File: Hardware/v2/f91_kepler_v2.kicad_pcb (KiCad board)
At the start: 2 copper layers, 25 x 27 mm, 89 parts, among them J1 LS013B7DH03 FPC, Q1 FS8205A, SW1 BTN1/BSL, SW2 BTN2, SW3 BTN3, U1 CC2652R7RGZ, U2 BQ51050B, U3 DW01A, U4 XC6206P302MR, U5 LIS2DW12, U6 DRV2605L, U7 ST25DV04K, Y1 48MHz FA-128, Y2 32.768kHz FC-135

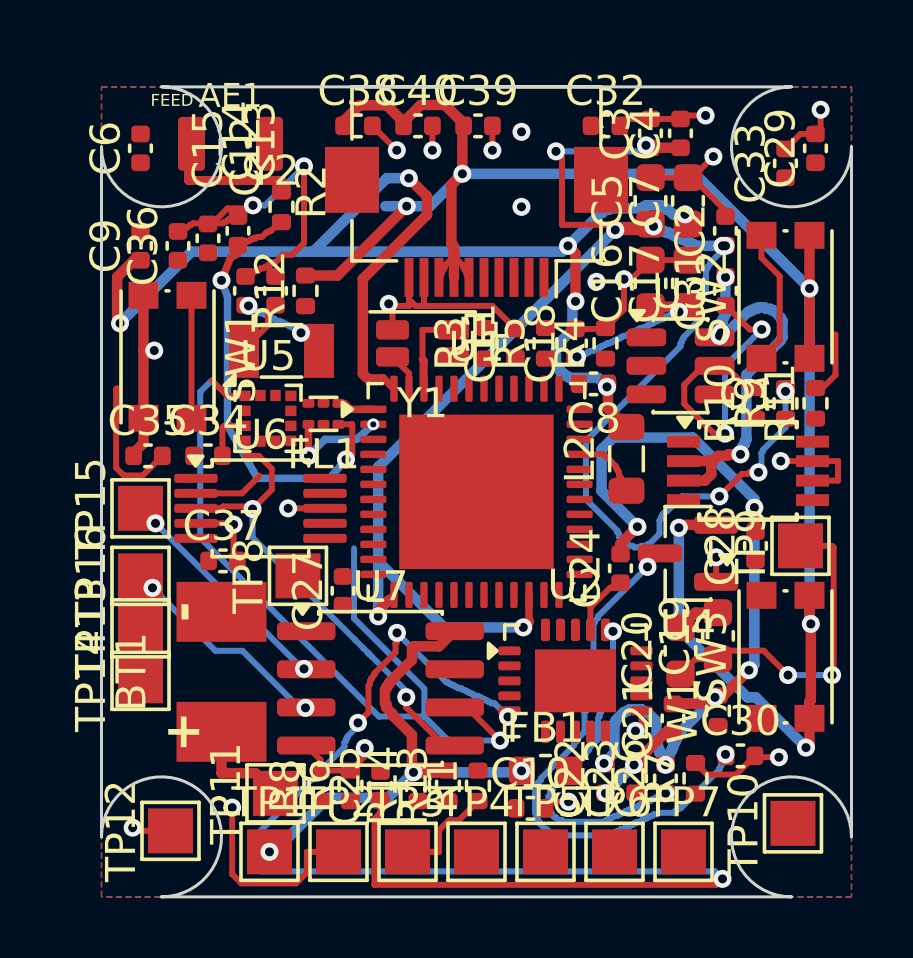
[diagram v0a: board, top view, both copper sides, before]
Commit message: feat(hw/v2): pin remap + placement surgery, routing at 54% remaining ratsnest
- re-pin (CC2652 IOC mux): LCD MOSI/SCLK/CS/DISP/EXTCOMIN -> DIO_27-30/26
  (top edge, face J1), BTN_1 -> DIO_0, BTN_3 -> DIO_20, UART_RX/TX ->
  DIO_9/10, ACC_INT2 -> DIO_11; schematic + board + kepler_config.h
  (KEPLER_BOARD_V2 block) + PINMAP.md all in sync, ERC 0
- surgery: U2 +0.7 (U1-U2 channel 0.35 -> 1.05mm), FB1/C22/C23/C26/R7
  cascade south, R3/C11/R5/C18/R4 row north (LCD via lane), U6 west,
  L2/C24 east (U1 right-col lanes), TP15/16 NFC taps into BT1 gap
  beside U7 NFC pins, Y2 north (HAPTIC_EN lane)
- clearance rules 0.2 -> 0.15 (JLC 0.127 capable), edge rule 0.22
- unconnected 198 -> 91; DRC clean except documented corner-arc phantom
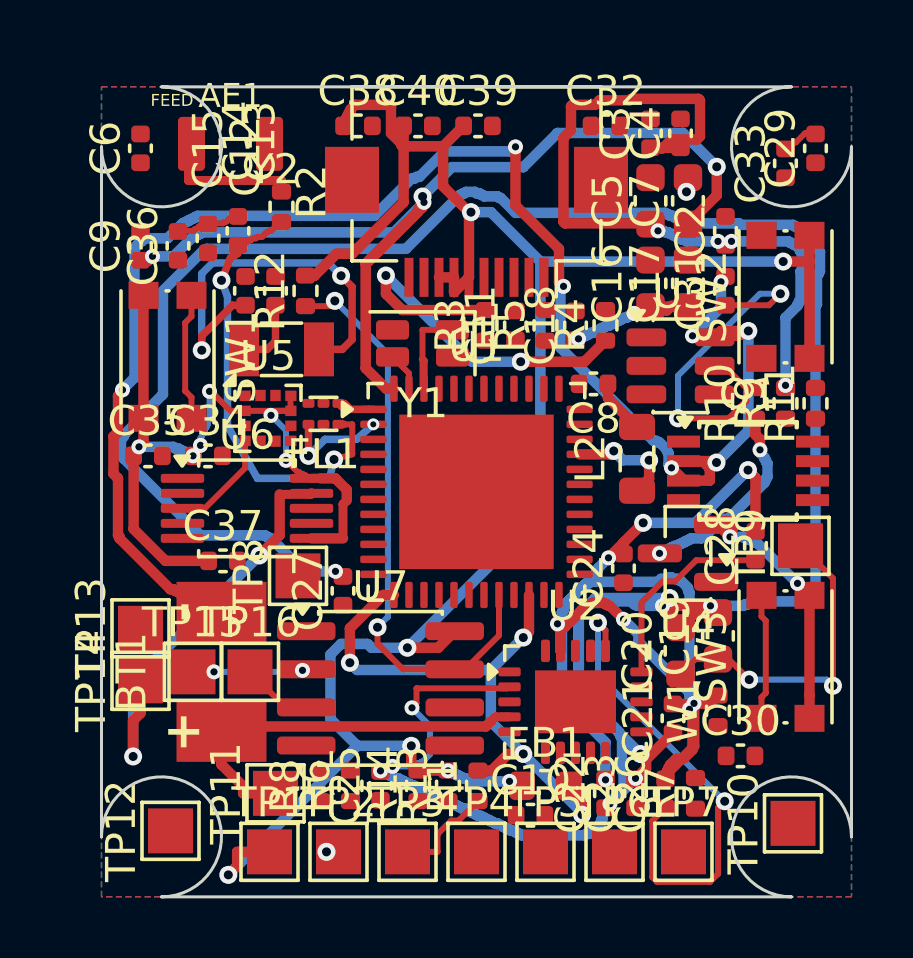
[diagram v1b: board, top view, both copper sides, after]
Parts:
- moved TP15 5.72 mm to (3.05, 19.5), turned to 0 degrees
- moved TP16 4.85 mm to (4.95, 19.5), turned to 0 degrees
- moved U2 0.70 mm to (15.8, 20.5)
- moved C11 0.60 mm to (13.8, 7.95)
- moved C18 0.60 mm to (15.8, 7.95)
- moved R3 0.60 mm to (12.8, 7.95)
- moved R4 0.60 mm to (16.8, 7.95)
- moved R5 0.60 mm to (14.8, 7.95)
- moved C22 0.50 mm to (16.8, 23.6)
- moved C23 0.50 mm to (17.8, 23.6)
- moved C26 0.50 mm to (18.8, 23.6)
- moved FB1 0.50 mm to (14.8, 23.3)
- moved R7 0.50 mm to (19.8, 23.6)
- moved U6 0.45 mm to (4.85, 14.1)
- moved L2 0.35 mm to (17.9, 12.4)
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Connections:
- U1 pad 14: ACC_INT2 -> unconnected-(U1-DIO_8-Pad14)
- U1 pad 15: LCD_MOSI -> UART_RX
- U1 pad 16: LCD_SCLK -> UART_TX
- U1 pad 17: LCD_CS -> ACC_INT2
- U1 pad 18: LCD_DISP -> unconnected-(U1-DIO_12-Pad18)
- U1 pad 19: LCD_EXTCOMIN -> unconnected-(U1-DIO_13-Pad19)
- U1 pad 21: BTN_1 -> unconnected-(U1-DIO_15-Pad21)
- U1 pad 30: unconnected-(U1-DIO_20-Pad30) -> BTN_3
- U1 pad 39: BTN_3 -> LCD_EXTCOMIN
- U1 pad 40: unconnected-(U1-DIO_27-Pad40) -> LCD_MOSI
- U1 pad 41: unconnected-(U1-DIO_28-Pad41) -> LCD_SCLK
- U1 pad 42: unconnected-(U1-DIO_29-Pad42) -> LCD_CS
- U1 pad 43: unconnected-(U1-DIO_30-Pad43) -> LCD_DISP
- U1 pad 5: unconnected-(U1-DIO_0-Pad5) -> BTN_1
- U1 pad 7: UART_RX -> unconnected-(U1-DIO_2-Pad7)
- U1 pad 8: UART_TX -> unconnected-(U1-DIO_3-Pad8)
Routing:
- net AC1: track 4.60 -> 98.2 mm, vias 2 -> 10
- net GND: track 68.2 -> 3.41 mm, vias 23 -> 2
- net CLAMP1: track 45.3 -> 0.00 mm, vias 4 -> 0
- net BATN: track 13.7 -> 55.3 mm, vias 4 -> 8
- net SCL: track 30.4 -> 0.00 mm, vias 1 -> 0
- net NFC_GPO: track 0.00 -> 19.6 mm, vias 0 -> 2
- net +3V0: track 91.7 -> 107.0 mm, vias 10 -> 15
- net MOT_N: track 0.00 -> 14.5 mm, vias 0 -> 2
- net VDDS: track 59.4 -> 45.6 mm, vias 11 -> 8
- net PIEZO: track 0.00 -> 12.9 mm, vias 0 -> 2
- net AC2: track 29.3 -> 41.9 mm, vias 6 -> 8
- net SDA: track 16.0 -> 3.55 mm, vias 2 -> 0
- net X32K_1: track 3.10 -> 13.4 mm
- net VDDR: track 44.9 -> 36.1 mm, vias 6 -> 4
- net COMM2: track 0.00 -> 6.69 mm
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
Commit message: feat(hw/v2): LCD-priority routing pass, lane capacity analysis
- north lane cleared + LCD_MOSI through; 91 -> 86 unconnected
- capacity arithmetic: 2-layer board oversubscribed (~20 nets vs ~11
  physical escape slots; via pitch 0.61 > pad pitch 0.5, single-track
  windows). Remaining 44 nets structurally blocked, not router-blocked
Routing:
- net COMM1: track 0.00 -> 17.0 mm, vias 0 -> 2
- net NFC_GPO: track 19.6 -> 8.31 mm
- net GND: track 3.41 -> 14.1 mm, vias 2 -> 6
- net PIEZO: track 12.9 -> 22.3 mm, vias 2 -> 5
- net PROT_OD: track 0.00 -> 8.28 mm, vias 0 -> 2
- net LCD_MOSI: track 0.00 -> 6.85 mm, vias 0 -> 2
- net BATN: track 55.3 -> 50.9 mm
- net +3V0: track 107.0 -> 102.9 mm, vias 15 -> 17
- net X48M_N: track 3.96 -> 2.96 mm
- net VDDR: track 36.1 -> 36.3 mm, vias 4 -> 6

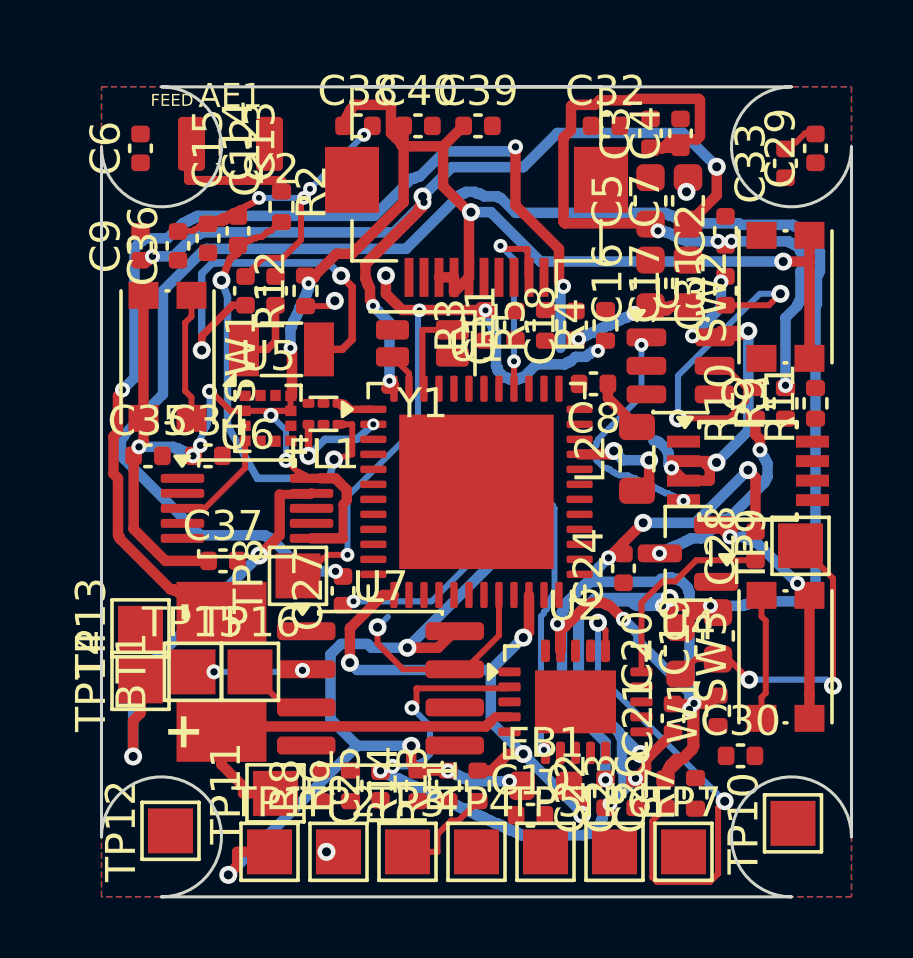
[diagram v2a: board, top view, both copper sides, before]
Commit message: feat(hw/v2): 4-layer conversion + rip-up router, 39 conns remain
Convert board to JLC04161H 4-layer stackup: In1.Cu solid GND plane,
In2.Cu routing layer, antenna keepout extended to inner layers.

- stackup4.py: layer conversion + GND_IN1 plane
- import_ses.py: inner-layer support, In1 wires dropped (plane integrity)
- grid_router.py: 3 routing layers, rip-up & retry with persistent
  congestion history, multi-layer endpoints, sub-grid bridges, GND
  zone-stub vias, separate pad inflation (0.5-pitch QFN escapes)
- stitch_gnd.py: GND stitching grid + per-fragment plane taps
- board: LCD corridor surgery (R3/C11 to NE corner), U1 EP 3x3 thermal
  via array, 53 stitching vias, Q1 clearance override removed

DRC: no real violations; 117 courtyard + corner-arc phantom edge
clearances pending documented exclusions. 39 connections unrouted
(fine-pitch escape pockets: Y1 pad blocks LCD_DISP/VDDR channels,
charger cluster pockets).
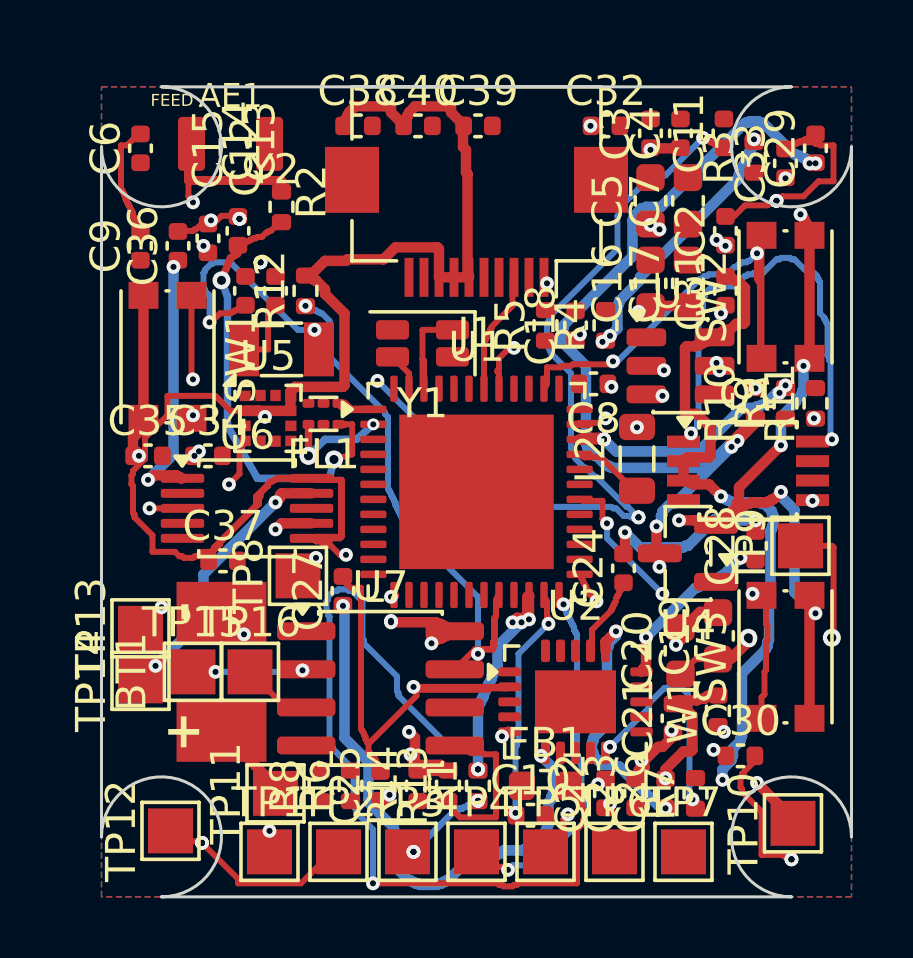
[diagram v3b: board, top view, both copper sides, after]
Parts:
- moved R3 10.6 mm to (21.8, 2.35)
- moved C11 9.45 mm to (20.8, 1.55)
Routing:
- net nRESET: track 3.40 -> 68.2 mm, vias 0 -> 9
- net AC1: track 98.2 -> 43.1 mm, vias 10 -> 5
- net +3V0: track 102.9 -> 155.3 mm, vias 17 -> 18
- net VDDR: track 36.3 -> 1.84 mm, vias 6 -> 2
- net VBAT: track 20.2 -> 48.8 mm, vias 2 -> 8
- net AC2: track 41.9 -> 15.6 mm, vias 8 -> 4
- net VDDS: track 45.6 -> 70.6 mm, vias 8 -> 16
- net BTN_2: track 0.00 -> 17.0 mm, vias 0 -> 2
- net FET_D: track 0.00 -> 16.1 mm, vias 0 -> 2
- net PROT_OC: track 0.00 -> 14.7 mm, vias 0 -> 2
- net GND: track 14.1 -> 27.7 mm, vias 6 -> 11
- net SWD_TMS: track 0.00 -> 12.4 mm, vias 0 -> 2
- net NFC_GPO: track 8.31 -> 20.0 mm
- net SWD_TCK: track 0.00 -> 10.2 mm, vias 0 -> 2
- net DRV_REG: track 0.00 -> 8.97 mm, vias 0 -> 2
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- added copper zone on In1.Cu, net GND
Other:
- copper layers 2 -> 4

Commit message: feat(hw/v2): via-in-pad exodus + exact-geometry hand routing, 29 conns remain
- 86 locked 0.4/0.2 via-in-pad ladders give walled endpoints In2/B access
- grid_router: endpoints inherit layers from own-net copper at their cell
- check_route.py: exact-geometry checker/emitter (rect pads, seg intersection,
  auto rip-list); hand-routed 30+ stubborn connections as locked routes
- VBAT 6-leg spine incl. B-layer grand tour BT1->NE; AC1/BTN_3/SWD_TMS/
  HAPTIC_EN/ILIM/FOD_TAP/TS/COMM1/SDA/SCL/VDDR/X32K_1/nRESET/PIEZO/BOOT1/
  CLAMP1/CLAMP2/CHG_DET routed by hand across F/In2/B
- gen_fab.sh: add In1.Cu/In2.Cu to gerber layer list
- DRC: 0 real violations (phantoms: corner-arc edge + courtyard only)
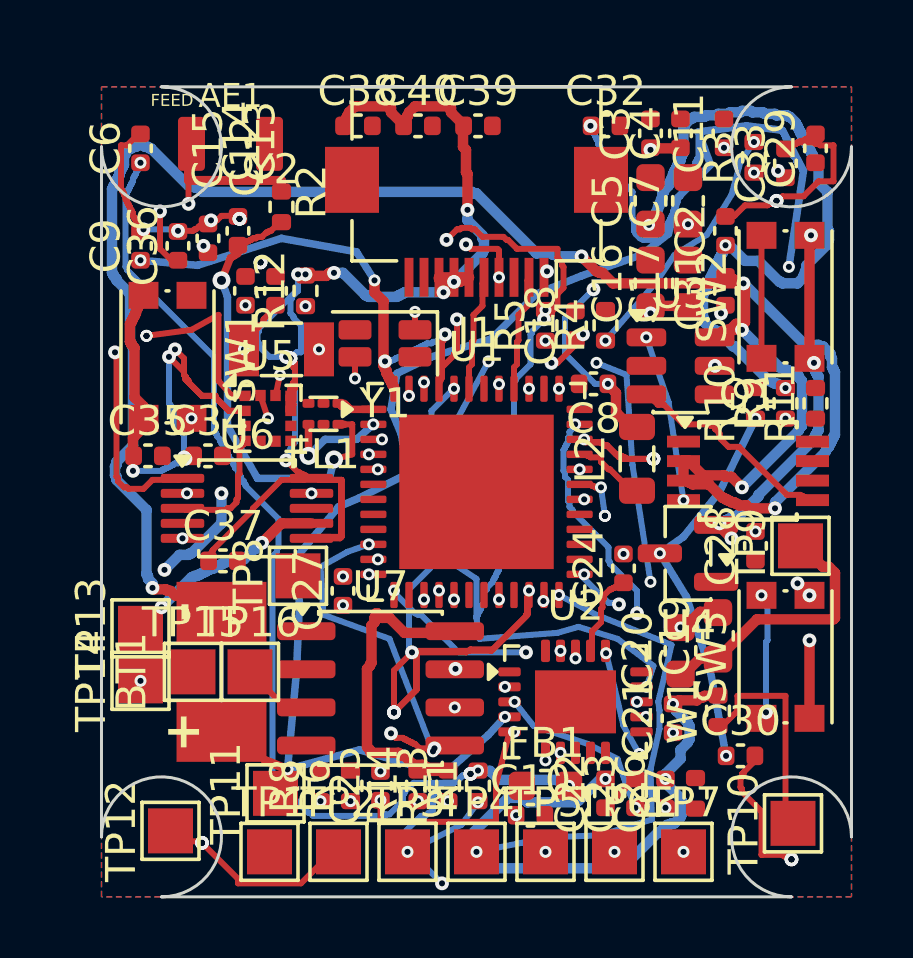
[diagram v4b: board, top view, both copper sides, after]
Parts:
- moved Y1 1.25 mm to (9.45, 8.55)
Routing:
- net VDDS: track 70.6 -> 155.7 mm, vias 16 -> 21
- net FOD_TAP: track 0.00 -> 66.2 mm, vias 0 -> 6
- net +3V0: track 155.3 -> 111.2 mm, vias 18 -> 23
- net VDDR: track 1.84 -> 40.2 mm, vias 2 -> 8
- net nRESET: track 68.2 -> 31.8 mm, vias 9 -> 5
- net VBAT: track 48.8 -> 85.0 mm, vias 8 -> 7
- net BATN: track 45.6 -> 68.6 mm, vias 3 -> 6
- net SCL: track 0.00 -> 18.1 mm, vias 0 -> 6
- net CHG_DET: track 0.00 -> 17.7 mm, vias 0 -> 5
- net AC1: track 43.1 -> 25.7 mm
- net NFC_GPO: track 20.0 -> 2.90 mm, vias 2 -> 3
- net FET_D: track 16.1 -> 0.00 mm, vias 2 -> 0
- net LCD_EXTCOMIN: track 0.00 -> 15.6 mm, vias 0 -> 3
- net HAPTIC_EN: track 0.00 -> 15.5 mm, vias 0 -> 2
- net ILIM: track 0.00 -> 14.6 mm, vias 0 -> 4
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
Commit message: wip: snapshot pre-migración
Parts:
- BT1: footprint f91_footprints:BatteryPads -> f91_footprints:Back_BatteryPads; moved to B.Cu
- C16, C17, C19, C20: footprint Capacitor_SMD:C_0603_1608Metric -> f91_footprints:Back_C_0603_1608Metric; moved to B.Cu
- C18, C21, C22, C23, C24, C25, C26, C27, C28, C29, C30, C31, C32, C33, C36, C37, C38: footprint Capacitor_SMD:C_0402_1005Metric -> f91_footprints:Back_C_0402_1005Metric; moved to B.Cu
- FL1: footprint f91_footprints:Murata_LFB18_1608 -> f91_footprints:F91_Murata_LFB18_1608
- J1: footprint Connector_FFC-FPC:Hirose_FH12-10S-0.5SH_1x10-1MP_P0.50mm_Horizontal -> f91_footprints:F91_LCD_FPC_Hirose_FH12-10
- Q1: footprint Package_SO:TSSOP-8_3x3mm_P0.65mm -> f91_footprints:Back_TSSOP-8_3x3mm_P0.65mm; moved to B.Cu
- R10, R11, R12, R13, R14, R5, R6, R7, R8, W1: footprint Resistor_SMD:R_0402_1005Metric -> f91_footprints:Back_R_0402_1005Metric; moved to B.Cu
- TP1, TP10, TP11, TP12, TP13, TP14, TP15, TP16, TP2, TP3, TP4, TP5, TP6, TP7, TP8, TP9: footprint TestPoint:TestPoint_Pad_1.5x1.5mm -> f91_footprints:Back_TestPoint_Pad_1.5x1.5mm; moved to B.Cu
- U2: footprint f91_footprints:VQFN-20-1EP_4.5x3.5mm_P0.5mm -> f91_footprints:Back_VQFN-20-1EP_4.5x3.5mm_P0.5mm; moved to B.Cu
- U3: footprint Package_TO_SOT_SMD:SOT-23-6 -> f91_footprints:Back_SOT-23-6; moved to B.Cu
- U4: footprint Package_TO_SOT_SMD:SOT-23 -> f91_footprints:Back_SOT-23; moved to B.Cu
- U6: footprint f91_footprints:VSSOP-10_3x3mm_P0.5mm -> f91_footprints:Back_VSSOP-10_3x3mm_P0.5mm; moved to B.Cu
- U7: footprint Package_SO:SOIC-8_3.9x4.9mm_P1.27mm -> f91_footprints:Back_SOIC-8_3.9x4.9mm_P1.27mm; moved to B.Cu
- Y1: footprint f91_footprints:Crystal_SMD_3215-4Pin_3.2x1.5mm -> f91_footprints:Epson_FA-128_2.0x1.6mm
- moved TP10 24.0 mm to (2.20, 12.6), turned to 0 degrees
- moved TP13 23.0 mm to (22.8, 10.0), turned to 0 degrees
- moved TP14 22.7 mm to (22.8, 12.6), turned to 0 degrees
- moved TP9 21.8 mm to (2.20, 10.0), turned to 0 degrees
- moved C6 20.2 mm to (10.6, 20.1), turned to 0 degrees
- moved C9 19.8 mm to (19.8, 12.3), turned to 0 degrees
- moved TP15 19.8 mm to (22.8, 20.0)
- moved C3 19.4 mm to (12.6, 20.1), turned to 0 degrees
- moved C4 18.5 mm to (15.1, 19.6), turned to 0 degrees
- moved BT1 18.1 mm to (12.5, 3.50), turned to 0 degrees
- moved C11 18.0 mm to (20.0, 19.5), turned to 0 degrees
- moved TP16 17.8 mm to (22.6, 22.0)
- moved R14 17.6 mm to (5.00, 6.65), turned to 0 degrees
- moved C30 17.1 mm to (13.2, 7.20)
- moved TP12 16.5 mm to (16.2, 15.9), turned to 0 degrees
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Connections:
- U1 pad 39: LCD_EXTCOMIN -> LCD_SCLK
- U1 pad 41: LCD_SCLK -> LCD_CS
- U1 pad 42: LCD_CS -> LCD_EXTCOMIN
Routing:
- net VDDS: track 155.7 -> 38.8 mm, vias 21 -> 2
- net FOD_TAP: track 66.2 -> 1.70 mm, vias 6 -> 0
- net VBAT: track 85.0 -> 28.2 mm, vias 7 -> 0
- net BATN: track 68.6 -> 20.9 mm, vias 6 -> 0
- net NFC_GPO: track 2.90 -> 42.2 mm, vias 3 -> 2
- net NFC_B: track 2.37 -> 39.4 mm, vias 0 -> 2
- net VDDR: track 40.2 -> 7.01 mm, vias 8 -> 1
- net NFC_A: track 0.00 -> 32.4 mm, vias 0 -> 2
- net UART_TX: track 0.00 -> 29.3 mm
- net DCOUPL: track 0.00 -> 28.6 mm
- net GND: track 29.0 -> 2.26 mm, vias 13 -> 107
- net AC2: track 20.8 -> 43.9 mm, vias 6 -> 2
- net PIEZO: track 8.45 -> 29.5 mm, vias 2 -> 5
- net SWD_TCK: track 20.1 -> 0.00 mm, vias 3 -> 0
- net CHG_DET: track 17.7 -> 0.00 mm, vias 5 -> 0
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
